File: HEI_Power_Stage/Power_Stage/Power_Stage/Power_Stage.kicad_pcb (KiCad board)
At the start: 2 copper layers, 1 part, among them Q1 EPC2304ENGRT

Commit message: second try for kicad libs
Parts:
- moved Q1 2.56 mm to (130.8, 83.4)
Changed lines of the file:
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@@
   (net 7 "unconnected-(Q1-Pad7)")
   (footprint "GTSR_KiCAD_Footprints_SD:EPC2304_ECC" (layer "F.Cu")
-    (at 133.298994 82.808311)
+    (at 130.798994 83.358311)
     (tags "EPC2304ENGRT ")
     (property "Sheetfile" "Power_Stage.kicad_sch")

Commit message: preliminary schematic and layout for POC
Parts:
- added C1: 3.3uF, GTSR_KiCAD_Footprints:CAP_6050_TDK, F.Cu at (105.0, 149.9)
- added C11: 15pF, Capacitor_SMD:C_0603_1608Metric_Pad1.08x0.95mm_HandSolder, F.Cu at (119.1, 121.2)
- added C12: 15pF, Capacitor_SMD:C_0603_1608Metric_Pad1.08x0.95mm_HandSolder, F.Cu at (120.3, 122.4)
- added C13: 1nF, Capacitor_SMD:C_0603_1608Metric_Pad1.08x0.95mm_HandSolder, F.Cu at (126.9, 136.0)
- added C14: 0.1uF, Capacitor_SMD:C_0603_1608Metric_Pad1.08x0.95mm_HandSolder, F.Cu at (124.0, 125.6)
- added C15: 1uF, Capacitor_SMD:C_0603_1608Metric_Pad1.08x0.95mm_HandSolder, F.Cu at (112.0, 125.2)
- added C16: 1uF, Capacitor_SMD:C_0603_1608Metric_Pad1.08x0.95mm_HandSolder, F.Cu at (118.2, 128.9)
- added C17: 470nF, Capacitor_SMD:C_0603_1608Metric_Pad1.08x0.95mm_HandSolder, F.Cu at (112.0, 123.6)
- added C18: 1uF, Capacitor_SMD:C_0603_1608Metric_Pad1.08x0.95mm_HandSolder, F.Cu at (116.3, 119.5)
- added C19: 0.1uF, Capacitor_SMD:C_0603_1608Metric_Pad1.08x0.95mm_HandSolder, F.Cu at (125.4, 145.0)
- added C2: 3.3uF, GTSR_KiCAD_Footprints:CAP_6050_TDK, F.Cu at (96.8, 127.0)
- added C20: 1uF, Capacitor_SMD:C_0603_1608Metric_Pad1.08x0.95mm_HandSolder, F.Cu at (124.9, 146.6)
- added C21: 0.1uF, Capacitor_SMD:C_0603_1608Metric_Pad1.08x0.95mm_HandSolder, F.Cu at (147.4, 146.6)
- added C23: 15pF, Capacitor_SMD:C_0603_1608Metric_Pad1.08x0.95mm_HandSolder, F.Cu at (145.1, 121.2)
- added C24: 15pF, Capacitor_SMD:C_0603_1608Metric_Pad1.08x0.95mm_HandSolder, F.Cu at (146.3, 122.4)
- added C25: 1nF, Capacitor_SMD:C_0603_1608Metric_Pad1.08x0.95mm_HandSolder, F.Cu at (152.9, 136.0)
- added C26: 0.1uF, Capacitor_SMD:C_0603_1608Metric_Pad1.08x0.95mm_HandSolder, F.Cu at (150.0, 125.6)
- added C27: 1uF, Capacitor_SMD:C_0603_1608Metric_Pad1.08x0.95mm_HandSolder, F.Cu at (138.0, 125.2)
- added C28: 1uF, Capacitor_SMD:C_0603_1608Metric_Pad1.08x0.95mm_HandSolder, F.Cu at (144.2, 128.9)
- added C29: 470nF, Capacitor_SMD:C_0603_1608Metric_Pad1.08x0.95mm_HandSolder, F.Cu at (138.0, 123.6)
- added C3: 3.3uF, GTSR_KiCAD_Footprints:CAP_6050_TDK, F.Cu at (104.0, 127.0)
- added C30: 1uF, Capacitor_SMD:C_0603_1608Metric_Pad1.08x0.95mm_HandSolder, F.Cu at (142.2, 119.5)
- added C31: 0.1uF, Capacitor_SMD:C_0603_1608Metric_Pad1.08x0.95mm_HandSolder, F.Cu at (151.4, 145.0)
- added C32: 1uF, Capacitor_SMD:C_0603_1608Metric_Pad1.08x0.95mm_HandSolder, F.Cu at (150.8, 146.6)
- added C33: 0.1uF, Capacitor_SMD:C_0603_1608Metric_Pad1.08x0.95mm_HandSolder, F.Cu at (173.4, 146.6)
- added C35: 15pF, Capacitor_SMD:C_0603_1608Metric_Pad1.08x0.95mm_HandSolder, F.Cu at (171.1, 121.2)
- added C36: 15pF, Capacitor_SMD:C_0603_1608Metric_Pad1.08x0.95mm_HandSolder, F.Cu at (172.3, 122.4)
- added C37: 1nF, Capacitor_SMD:C_0603_1608Metric_Pad1.08x0.95mm_HandSolder, F.Cu at (178.9, 136.0)
- added C38: 0.1uF, Capacitor_SMD:C_0603_1608Metric_Pad1.08x0.95mm_HandSolder, F.Cu at (176.0, 125.6)
- added C39: 1uF, Capacitor_SMD:C_0603_1608Metric_Pad1.08x0.95mm_HandSolder, F.Cu at (164.0, 125.2)
- added C40: 1uF, Capacitor_SMD:C_0603_1608Metric_Pad1.08x0.95mm_HandSolder, F.Cu at (170.1, 128.9)
- added C41: 470nF, Capacitor_SMD:C_0603_1608Metric_Pad1.08x0.95mm_HandSolder, F.Cu at (164.0, 123.6)
- added C42: 1uF, Capacitor_SMD:C_0603_1608Metric_Pad1.08x0.95mm_HandSolder, F.Cu at (168.2, 119.5)
- added C43: 0.1uF, Capacitor_SMD:C_0603_1608Metric_Pad1.08x0.95mm_HandSolder, F.Cu at (177.4, 145.0)
- added C44: 1uF, Capacitor_SMD:C_0603_1608Metric_Pad1.08x0.95mm_HandSolder, F.Cu at (176.8, 146.6)
- added C6: 10uF, Capacitor_SMD:C_0603_1608Metric_Pad1.08x0.95mm_HandSolder, F.Cu at (132.0, 109.0)
- added C7: 10uF, Capacitor_SMD:C_0603_1608Metric_Pad1.08x0.95mm_HandSolder, F.Cu at (116.0, 105.6)
- added C8: 10uF, Capacitor_SMD:C_0603_1608Metric_Pad1.08x0.95mm_HandSolder, F.Cu at (127.1, 116.6)
- added C9: 0.1uF, Capacitor_SMD:C_0603_1608Metric_Pad1.08x0.95mm_HandSolder, F.Cu at (121.4, 146.6)
- added D2: G, LED_SMD:LED_0603_1608Metric_Pad1.05x0.95mm_HandSolder, F.Cu at (116.0, 114.0)
- added D3: RFU02VSM6STR, GTSR_KiCAD_Footprints:DIO_RFU02VS_ROM-M, F.Cu at (114.3, 120.7)
- added D4: RFU02VSM6STR, GTSR_KiCAD_Footprints:DIO_RFU02VS_ROM-M, F.Cu at (140.3, 120.7)
- added D5: RFU02VSM6STR, GTSR_KiCAD_Footprints:DIO_RFU02VS_ROM-M, F.Cu at (166.3, 120.7)
- added H1: No. 8, MountingHole:MountingHole_2.1mm, F.Cu at (188.0, 105.5)
- added H2: No. 8, MountingHole:MountingHole_2.1mm, F.Cu at (96.0, 105.5)
- added H3: No. 8, MountingHole:MountingHole_2.1mm, F.Cu at (188.0, 151.2)
- added H4: No. 8, MountingHole:MountingHole_2.1mm, F.Cu at (96.0, 151.5)
- added J1: OSTTA020161, GTSR_KiCAD_Footprints:CONN_OSTTA020161_OST, F.Cu at (97.3, 135.1)
- added J2: Conn_02x10_Odd_Even, Connector_PinSocket_2.54mm:PinSocket_2x10_P2.54mm_Horizontal, F.Cu at (158.2, 106.5)
- added J3: Screw_Terminal_01x01, GTSR_KiCAD_Footprints_SD:CONN6_1057_WRE, F.Cu at (116.9, 147.4)
- added J4: Screw_Terminal_01x01, GTSR_KiCAD_Footprints_SD:CONN6_1057_WRE, F.Cu at (137.8, 152.5)
- added J5: Screw_Terminal_01x01, GTSR_KiCAD_Footprints_SD:CONN6_1057_WRE, F.Cu at (163.8, 152.5)
- added Q2: EPC2304ENGRT, GTSR_KiCAD_Footprints:EPC2304_ECC, F.Cu at (119.0, 134.7)
- added Q3: EPC2304ENGRT, GTSR_KiCAD_Footprints:EPC2304_ECC, F.Cu at (135.7, 134.7)
- added Q4: EPC2304ENGRT, GTSR_KiCAD_Footprints:EPC2304_ECC, F.Cu at (145.0, 134.7)
- added Q5: EPC2304ENGRT, GTSR_KiCAD_Footprints:EPC2304_ECC, F.Cu at (161.7, 134.7)
- added Q6: EPC2304ENGRT, GTSR_KiCAD_Footprints:EPC2304_ECC, F.Cu at (171.0, 134.7)
- added R10: 10k, Resistor_SMD:R_1206_3216Metric, F.Cu at (124.7, 150.0)
- added R11: 10k, Resistor_SMD:R_0603_1608Metric_Pad0.98x0.95mm_HandSolder, F.Cu at (131.2, 147.2)
- added R12: 0.47 1/16W, Resistor_SMD:R_0603_1608Metric_Pad0.98x0.95mm_HandSolder, F.Cu at (111.4, 128.9)
- added R13: 0 1/16W, Resistor_SMD:R_0603_1608Metric_Pad0.98x0.95mm_HandSolder, F.Cu at (113.1, 128.9)
- added R14: 0.47 1/16W, Resistor_SMD:R_0603_1608Metric_Pad0.98x0.95mm_HandSolder, F.Cu at (120.7, 128.9)
- added R15: 0 1/16W, Resistor_SMD:R_0603_1608Metric_Pad0.98x0.95mm_HandSolder, F.Cu at (122.4, 128.9)
- added R16: 330, Resistor_SMD:R_0603_1608Metric_Pad0.98x0.95mm_HandSolder, F.Cu at (125.3, 136.0)
- added R18: 2.2 0.1W, Resistor_SMD:R_0603_1608Metric_Pad0.98x0.95mm_HandSolder, F.Cu at (145.2, 118.8)
- added R19: 2.2 0.1W, Resistor_SMD:R_0603_1608Metric_Pad0.98x0.95mm_HandSolder, F.Cu at (148.7, 122.3)
- added R2: 440, Resistor_SMD:R_0603_1608Metric_Pad0.98x0.95mm_HandSolder, F.Cu at (116.0, 110.0)
- added R20: 50k, Resistor_SMD:R_0603_1608Metric_Pad0.98x0.95mm_HandSolder, F.Cu at (148.9, 124.4)
- added R21: 10k, Resistor_SMD:R_0603_1608Metric_Pad0.98x0.95mm_HandSolder, F.Cu at (155.5, 147.2)
- added R22: 2 1/16W, Resistor_SMD:R_0603_1608Metric_Pad0.98x0.95mm_HandSolder, F.Cu at (137.2, 121.9)
- added R23: 715k, Resistor_SMD:R_1206_3216Metric, F.Cu at (147.4, 150.0)
- added R24: 10k, Resistor_SMD:R_1206_3216Metric, F.Cu at (150.7, 150.0)
- added R25: 10k, Resistor_SMD:R_0603_1608Metric_Pad0.98x0.95mm_HandSolder, F.Cu at (157.2, 147.2)
- added R26: 0.47 1/16W, Resistor_SMD:R_0603_1608Metric_Pad0.98x0.95mm_HandSolder, F.Cu at (137.4, 128.9)
- added R27: 0 1/16W, Resistor_SMD:R_0603_1608Metric_Pad0.98x0.95mm_HandSolder, F.Cu at (139.1, 128.9)
- added R28: 0.47 1/16W, Resistor_SMD:R_0603_1608Metric_Pad0.98x0.95mm_HandSolder, F.Cu at (146.7, 128.9)
- added R29: 0 1/16W, Resistor_SMD:R_0603_1608Metric_Pad0.98x0.95mm_HandSolder, F.Cu at (148.4, 128.9)
- added R30: 330, Resistor_SMD:R_0603_1608Metric_Pad0.98x0.95mm_HandSolder, F.Cu at (151.3, 136.0)
- added R32: 2.2 0.1W, Resistor_SMD:R_0603_1608Metric_Pad0.98x0.95mm_HandSolder, F.Cu at (171.2, 118.8)
- added R33: 2.2 0.1W, Resistor_SMD:R_0603_1608Metric_Pad0.98x0.95mm_HandSolder, F.Cu at (174.7, 122.3)
- added R34: 50k, Resistor_SMD:R_0603_1608Metric_Pad0.98x0.95mm_HandSolder, F.Cu at (174.9, 124.4)
- added R35: 10k, Resistor_SMD:R_0603_1608Metric_Pad0.98x0.95mm_HandSolder, F.Cu at (181.5, 147.2)
- added R36: 2 1/16W, Resistor_SMD:R_0603_1608Metric_Pad0.98x0.95mm_HandSolder, F.Cu at (163.1, 121.9)
- added R37: 715k, Resistor_SMD:R_1206_3216Metric, F.Cu at (173.4, 150.0)
- added R38: 10k, Resistor_SMD:R_1206_3216Metric, F.Cu at (176.6, 150.0)
- added R39: 10k, Resistor_SMD:R_0603_1608Metric_Pad0.98x0.95mm_HandSolder, F.Cu at (183.1, 147.2)
- added R4: 2.2 0.1W, Resistor_SMD:R_0603_1608Metric_Pad0.98x0.95mm_HandSolder, F.Cu at (119.2, 118.8)
- added R40: 0.47 1/16W, Resistor_SMD:R_0603_1608Metric_Pad0.98x0.95mm_HandSolder, F.Cu at (163.4, 128.9)
- added R41: 0 1/16W, Resistor_SMD:R_0603_1608Metric_Pad0.98x0.95mm_HandSolder, F.Cu at (165.1, 128.9)
- added R42: 0.47 1/16W, Resistor_SMD:R_0603_1608Metric_Pad0.98x0.95mm_HandSolder, F.Cu at (172.7, 128.9)
- added R43: 0 1/16W, Resistor_SMD:R_0603_1608Metric_Pad0.98x0.95mm_HandSolder, F.Cu at (174.4, 128.9)
- added R44: 330, Resistor_SMD:R_0603_1608Metric_Pad0.98x0.95mm_HandSolder, F.Cu at (177.3, 136.0)
- added R5: 2.2 0.1W, Resistor_SMD:R_0603_1608Metric_Pad0.98x0.95mm_HandSolder, F.Cu at (122.7, 122.3)
- added R6: 50k, Resistor_SMD:R_0603_1608Metric_Pad0.98x0.95mm_HandSolder, F.Cu at (122.9, 124.4)
- added R7: 10k, Resistor_SMD:R_0603_1608Metric_Pad0.98x0.95mm_HandSolder, F.Cu at (129.5, 147.2)
- added R8: 2 1/16W, Resistor_SMD:R_0603_1608Metric_Pad0.98x0.95mm_HandSolder, F.Cu at (111.2, 121.9)
- added R9: 715k, Resistor_SMD:R_1206_3216Metric, F.Cu at (121.4, 150.0)
- added T1: 30k, GTSR_KiCAD_Footprints_SD:2152723803, F.Cu at (129.7, 152.8)
- added T2: 30k, GTSR_KiCAD_Footprints_SD:2152723803, F.Cu at (129.7, 149.8)
- added T3: 30k, GTSR_KiCAD_Footprints_SD:2152723803, F.Cu at (155.7, 152.8)
- added T4: 30k, GTSR_KiCAD_Footprints_SD:2152723803, F.Cu at (155.7, 149.8)
- added T5: 30k, GTSR_KiCAD_Footprints_SD:2152723803, F.Cu at (181.6, 152.8)
- added T6: 30k, GTSR_KiCAD_Footprints_SD:2152723803, F.Cu at (181.6, 149.8)
- added TP1: Test_Point, TestPoint:TestPoint_Pad_D1.0mm, F.Cu at (135.3, 113.0)
- added TP10: Test_Point, TestPoint:TestPoint_Pad_D1.0mm, F.Cu at (174.2, 131.7)
- added TP2: Test_Point, TestPoint:TestPoint_Pad_D1.0mm, F.Cu at (132.0, 113.0)
- added TP5: Test_Point, TestPoint:TestPoint_Pad_D1.0mm, F.Cu at (112.9, 131.7)
- added TP6: Test_Point, TestPoint:TestPoint_Pad_D1.0mm, F.Cu at (122.2, 131.7)
- added TP7: Test_Point, TestPoint:TestPoint_Pad_D1.0mm, F.Cu at (138.9, 131.7)
- added TP8: Test_Point, TestPoint:TestPoint_Pad_D1.0mm, F.Cu at (148.2, 131.7)
- added TP9: Test_Point, TestPoint:TestPoint_Pad_D1.0mm, F.Cu at (164.9, 131.7)
- added U10: ~, GTSR_KiCAD_Footprints_SD:XDCR_ACS72981LLRATR-100B5, F.Cu at (172.0, 142.0)
- added U11: NCP51820AMNTWG, GTSR_KiCAD_Footprints:QFN_0AMNTWG_ONS-L, F.Cu at (168.9, 125.0)
- added U12: ADC124S051CIMM/NOPB, GTSR_KiCAD_Footprints:SOP50P490X110-10N, F.Cu at (177.5, 141.0)
- added U2: 1769205241, GTSR_KiCAD_Footprints_SD:176920512, F.Cu at (123.9, 108.6)
- added U3: TPS73250DBVR, Package_TO_SOT_SMD:TSOT-23-5, F.Cu at (128.0, 120.0)
- added U4: ~, GTSR_KiCAD_Footprints_SD:XDCR_ACS72981LLRATR-100B5, F.Cu at (120.0, 142.0)
- added U5: NCP51820AMNTWG, GTSR_KiCAD_Footprints:QFN_0AMNTWG_ONS-L, F.Cu at (116.9, 125.0)
- added U6: ADC124S051CIMM/NOPB, GTSR_KiCAD_Footprints:SOP50P490X110-10N, F.Cu at (125.5, 141.0)
- added U7: ~, GTSR_KiCAD_Footprints_SD:XDCR_ACS72981LLRATR-100B5, F.Cu at (146.0, 142.0)
- added U8: NCP51820AMNTWG, GTSR_KiCAD_Footprints:QFN_0AMNTWG_ONS-L, F.Cu at (142.9, 125.0)
- added U9: ADC124S051CIMM/NOPB, GTSR_KiCAD_Footprints:SOP50P490X110-10N, F.Cu at (151.5, 141.0)
- Q1: footprint GTSR_KiCAD_Footprints_SD:EPC2304_ECC -> GTSR_KiCAD_Footprints:EPC2304_ECC
- moved Q1 55.5 mm to (109.7, 134.7)
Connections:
- Q1 pad 1: unconnected-(Q1-Pad1) -> /Phase1/HS_{Gate}
- Q1 pad 2: unconnected-(Q1-Pad2) -> /Phase1/SW
- Q1 pad 3: unconnected-(Q1-Pad3) -> VDC
- Q1 pad 4: unconnected-(Q1-Pad4) -> /Phase1/SW
- Q1 pad 5: unconnected-(Q1-Pad5) -> VDC
- Q1 pad 6: unconnected-(Q1-Pad6) -> /Phase1/SW
- Q1 pad 7: unconnected-(Q1-Pad7) -> VDC
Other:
- board outline added: 100 x 56 mm

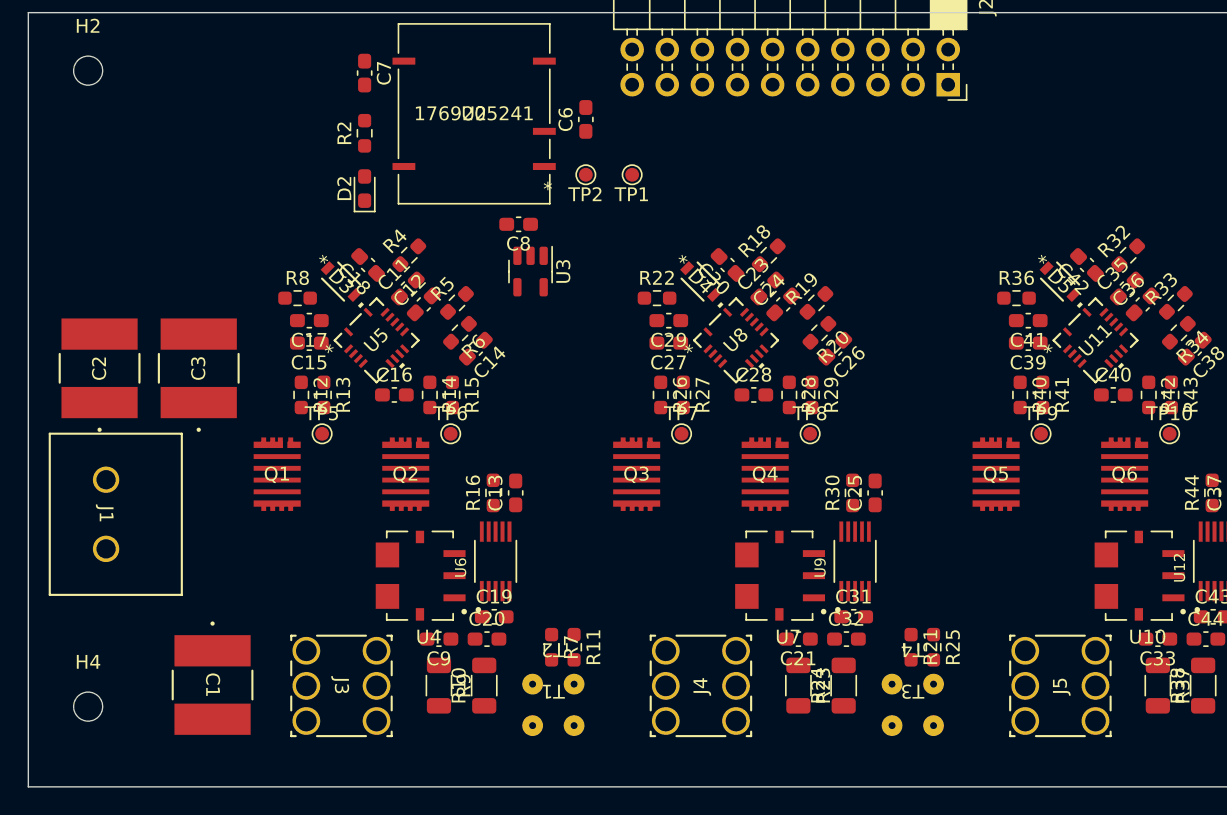
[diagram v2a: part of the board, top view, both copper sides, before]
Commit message: initial phase a routing
routed connections for phase A not including SPI. spi left as stubs that can be routed to connector and to the other ADCs.
Power and PWRGND routing is done on layer 1,2,4 and can be discussed further in persons. For now I have VDC on layer 1 and 4. PWRGND on layer 1 and 4. SW and PHA on layer 1 and 2. layer 3 and 5 are gnd. Layer 1 and 6 are signal.
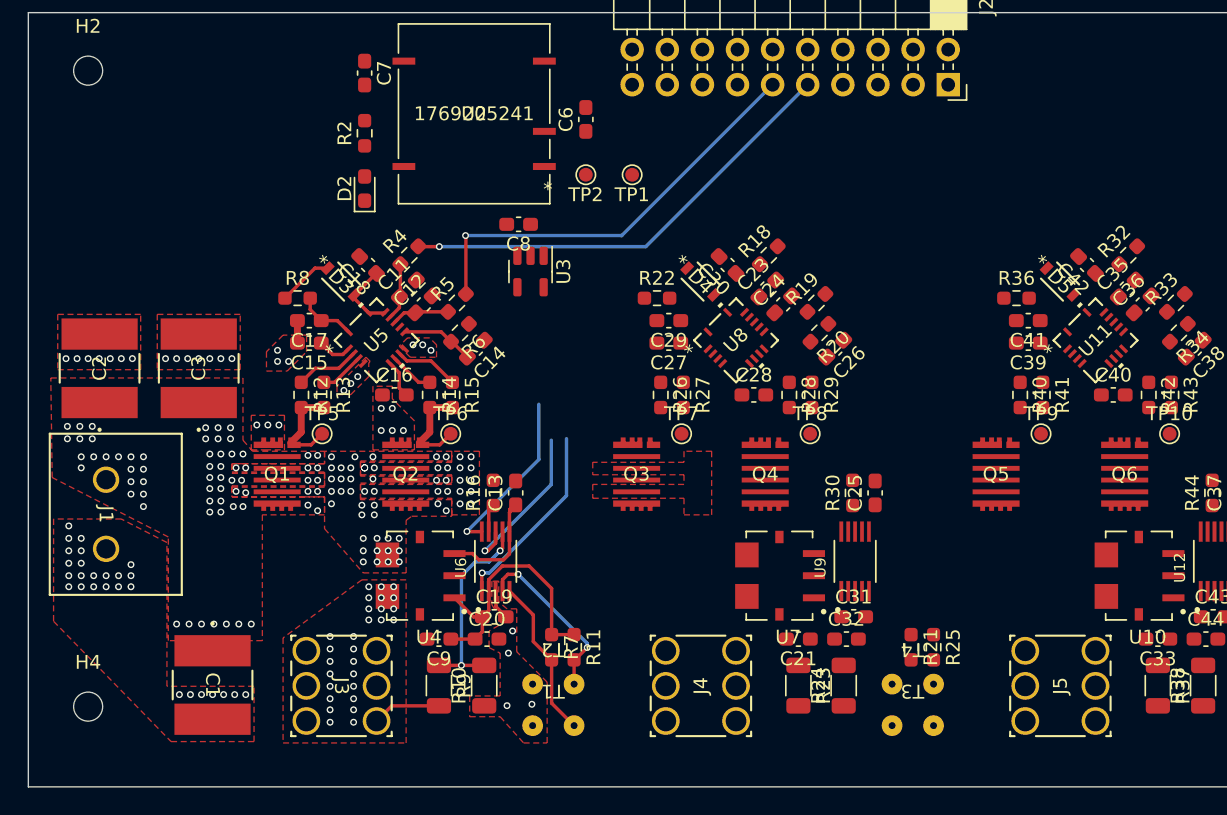
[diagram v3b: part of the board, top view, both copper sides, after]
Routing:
- net /AHS_{PWM}: track 0.00 -> 33.1 mm, vias 0 -> 1
- net /ALS_{PWM}: track 0.00 -> 31.0 mm, vias 0 -> 1
- net /5Vref: track 0.00 -> 19.6 mm
- net /Phase1/V_{sense}: track 0.00 -> 14.8 mm, vias 0 -> 2
- net /A~{CS}: track 0.00 -> 13.9 mm, vias 0 -> 1
- net /Phase1/LS_{Tsense}: track 0.00 -> 12.6 mm, vias 0 -> 2
- net /CLK: track 0.00 -> 12.4 mm, vias 0 -> 1
- net /MOSI: track 0.00 -> 11.8 mm, vias 0 -> 1
- net /Phase1/HS_{Tsense}: track 0.00 -> 11.7 mm
- net /Phase1/I_{sense}: track 0.00 -> 8.13 mm
- net /Phase1/HS_{Gate}: track 0.00 -> 6.86 mm
- net /Phase1/LS_{Gate}: track 0.00 -> 6.86 mm
- net /Phase1/DT: track 0.00 -> 5.30 mm
- net +12V: track 0.00 -> 5.16 mm
- net /PHA: track 0.00 -> 4.97 mm, vias 0 -> 28
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- added copper zone on F.Cu, net /PHA
- added copper zone on In1.Cu, net /PHA
- added copper zone on F.Cu, net /Phase1/SW
- added copper zone on In1.Cu, net /Phase1/SW
- added copper zone on F.Cu, net GNDPWR
- added copper zone on In1.Cu, net GNDPWR
- added copper zone on In3.Cu, net GNDPWR
- added copper zone on F.Cu, net VDC
- added copper zone on In3.Cu, net VDC
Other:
- copper layers 2 -> 6

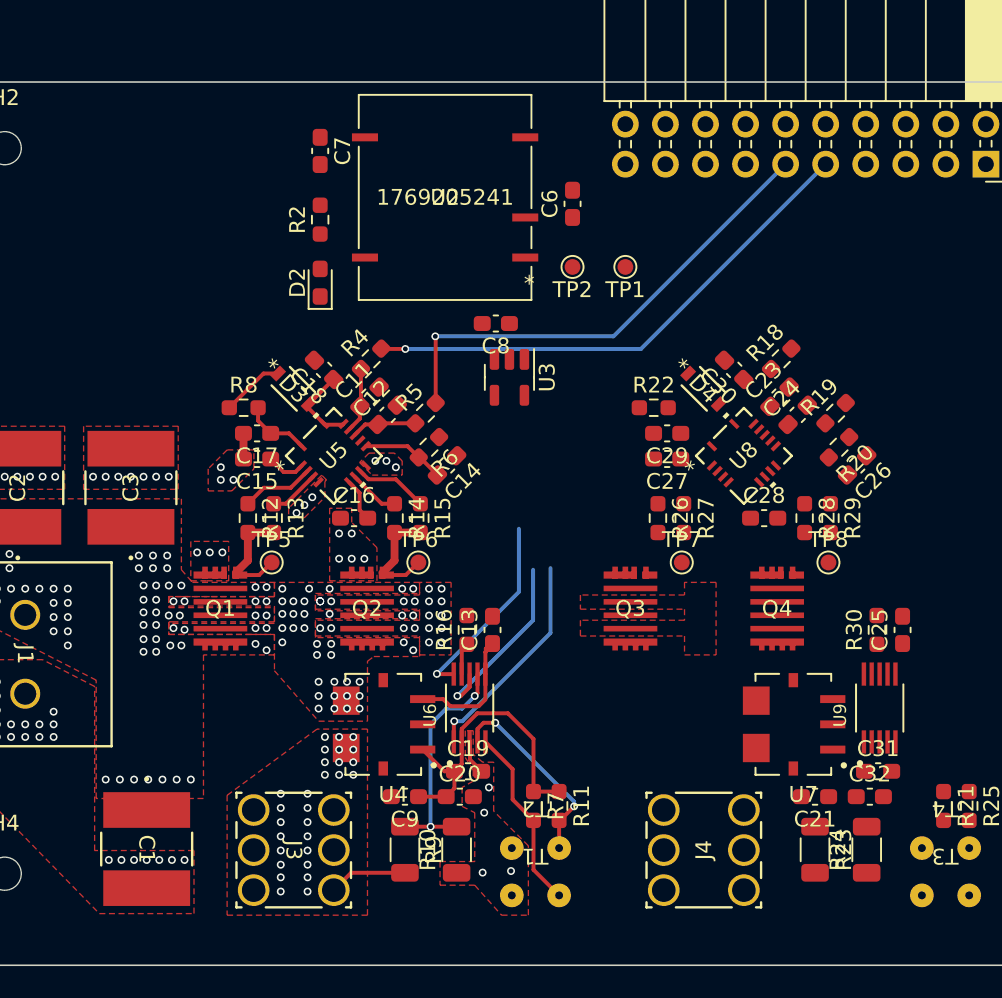
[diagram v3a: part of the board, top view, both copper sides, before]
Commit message: SPI and ldo
wired spi and ldo, thinking about stackup layer assignments for power. Layer 4 could be all VDC and PWD GND only, routing VDC on the top half and PWRGND on the bottom half. Then layer 1,2 can be for switch nodes and kelvin source returns and stuff. also thinking all more sensitive signals like 5vref should go on the bottom layer because layer 5 is solid gnd
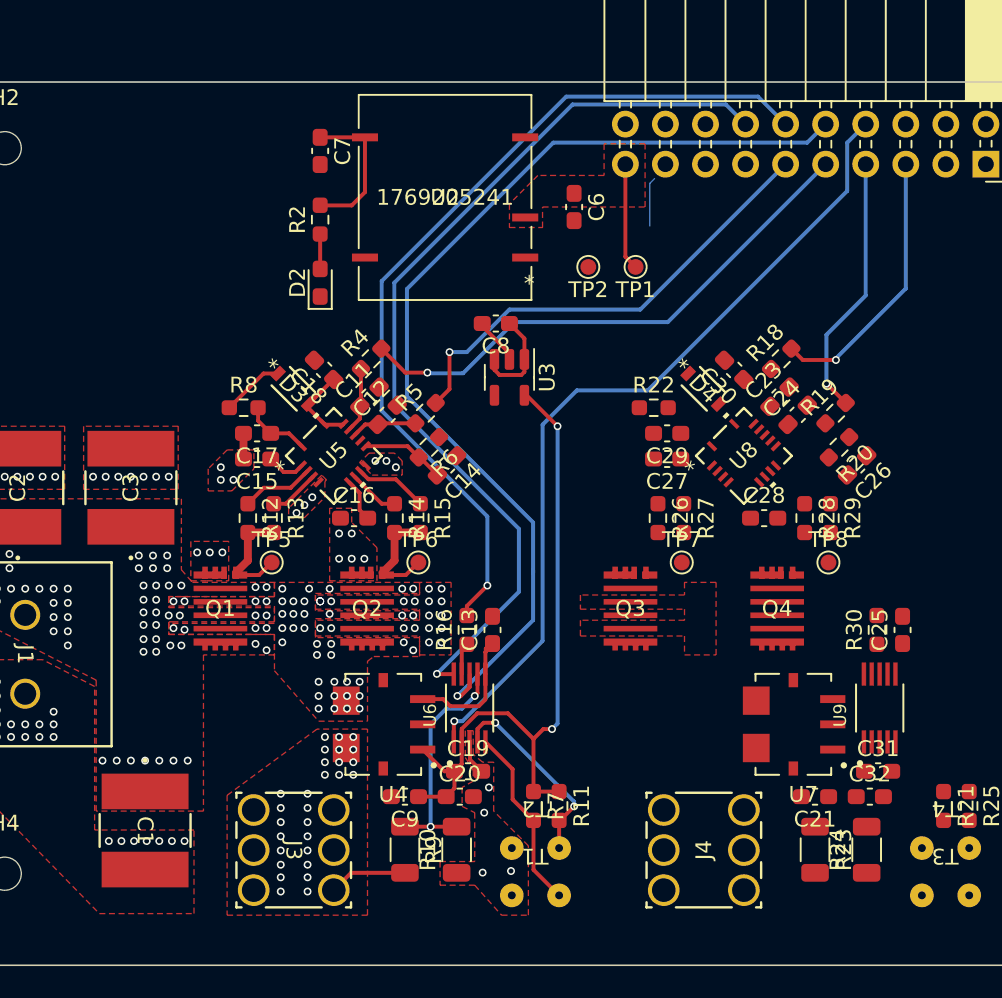
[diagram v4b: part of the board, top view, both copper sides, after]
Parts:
- moved C1 1.18 mm to (104.9, 148.7)
- moved TP2 1.00 mm to (133.0, 113.0)
- moved TP1 0.65 mm to (136.0, 113.0)
- moved C6 0.22 mm to (132.1, 109.2), turned to -90 degrees
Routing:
- net /MISO: track 0.00 -> 55.7 mm, vias 0 -> 1
- net /MOSI: track 11.8 -> 64.0 mm
- net /CLK: track 12.4 -> 58.8 mm
- net /A~{CS}: track 13.9 -> 52.9 mm
- net /5Vref: track 19.6 -> 43.3 mm, vias 0 -> 2
- net /BHS_{PWM}: track 0.00 -> 17.4 mm, vias 0 -> 1
- net /BLS_{PWM}: track 0.00 -> 16.7 mm, vias 0 -> 1
- net +5V: track 0.00 -> 15.7 mm
- net +12V: track 5.16 -> 11.9 mm
- net (no net): track 0.00 -> 3.12 mm
- net GNDPWR: track 2.38 -> 5.37 mm
- net Net-(D2-A): track 0.00 -> 2.21 mm
- net /AHS_{PWM}: track 33.1 -> 34.4 mm
- net /ALS_{PWM}: track 31.0 -> 29.8 mm
- added copper zone on F.Cu, net +12V

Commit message: changes in meeting
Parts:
- added C4: 10uF, Capacitor_SMD:C_0603_1608Metric_Pad1.08x0.95mm_HandSolder, F.Cu at (166.5, 104.9)
- added C5: 10uF, Capacitor_SMD:C_0603_1608Metric_Pad1.08x0.95mm_HandSolder, F.Cu at (166.5, 107.4)
- added D1: G, LED_SMD:LED_0603_1608Metric_Pad1.05x0.95mm_HandSolder, F.Cu at (170.9, 111.0)
- added R1: 1.8k, Resistor_SMD:R_0603_1608Metric_Pad0.98x0.95mm_HandSolder, F.Cu at (166.5, 109.9)
- added TP3: Test_Point, TestPoint:TestPoint_Pad_D1.0mm, F.Cu at (170.2, 105.1)
- added TP4: Test_Point, TestPoint:TestPoint_Pad_D1.0mm, F.Cu at (170.2, 108.2)
- J2: footprint Connector_PinSocket_2.54mm:PinSocket_2x10_P2.54mm_Horizontal -> Connector_PinHeader_2.54mm:PinHeader_2x10_P2.54mm_Horizontal
- moved U3 34.8 mm to (125.8, 154.7)
- moved J2 22.8 mm to (135.4, 107.0), turned to 90 degrees
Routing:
- net /MOSI: track 64.0 -> 1.83 mm
- net /CLK: track 58.8 -> 1.08 mm
- net /MISO: track 55.7 -> 2.44 mm
- net /A~{CS}: track 52.9 -> 1.33 mm
- net /AHS_{PWM}: track 34.4 -> 3.55 mm
- net /ALS_{PWM}: track 29.8 -> 3.59 mm
- net /5Vref: track 43.3 -> 24.0 mm
- net /BLS_{PWM}: track 16.7 -> 1.73 mm
- net /BHS_{PWM}: track 17.4 -> 3.12 mm
- net /Phase1/V_{sense}: track 14.8 -> 4.73 mm
- net /Phase1/LS_{Tsense}: track 12.6 -> 5.19 mm
- net (no net): track 3.12 -> 0.00 mm
- net VDC: vias 57 -> 51
- net /Phase1/SW: vias 53 -> 52
- removed copper zone on In3.Cu, net GNDPWR
- removed copper zone on In3.Cu, net VDC
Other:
- copper layers 6 -> 4

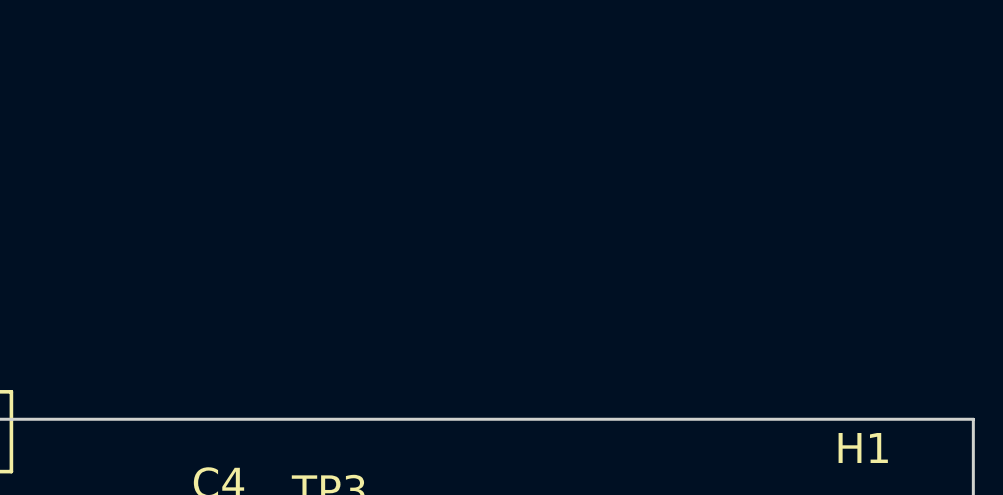
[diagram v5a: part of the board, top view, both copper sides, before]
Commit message: added 12-12 footprint
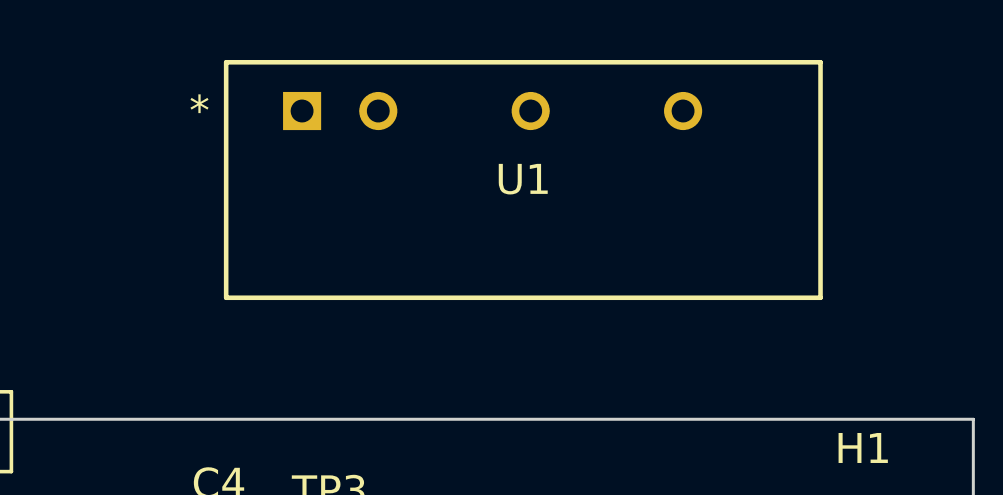
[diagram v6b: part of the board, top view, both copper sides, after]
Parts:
- added U1: TBA 2-1212, GTSR_KiCAD_Footprints_SD:TBA 2_SINGLE_TRP, F.Cu at (169.3, 91.0)
